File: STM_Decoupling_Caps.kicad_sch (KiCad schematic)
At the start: 11 parts

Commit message: Layout draft complete
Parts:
- added C78: 100 nF, Capacitor_SMD:C_0603_1608Metric, symbol Device:C
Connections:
- net GND: now also C78.1
- new net STM_NRST: C78.2
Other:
- note added: "NRST"
- note added: "VDDA-14"
- note added: "VREF-13"
- title: (none) -> Jakka1
- moved on the sheet: C5, C61, C62, C63, C64, C65, C66, C67, C68, C69, C70

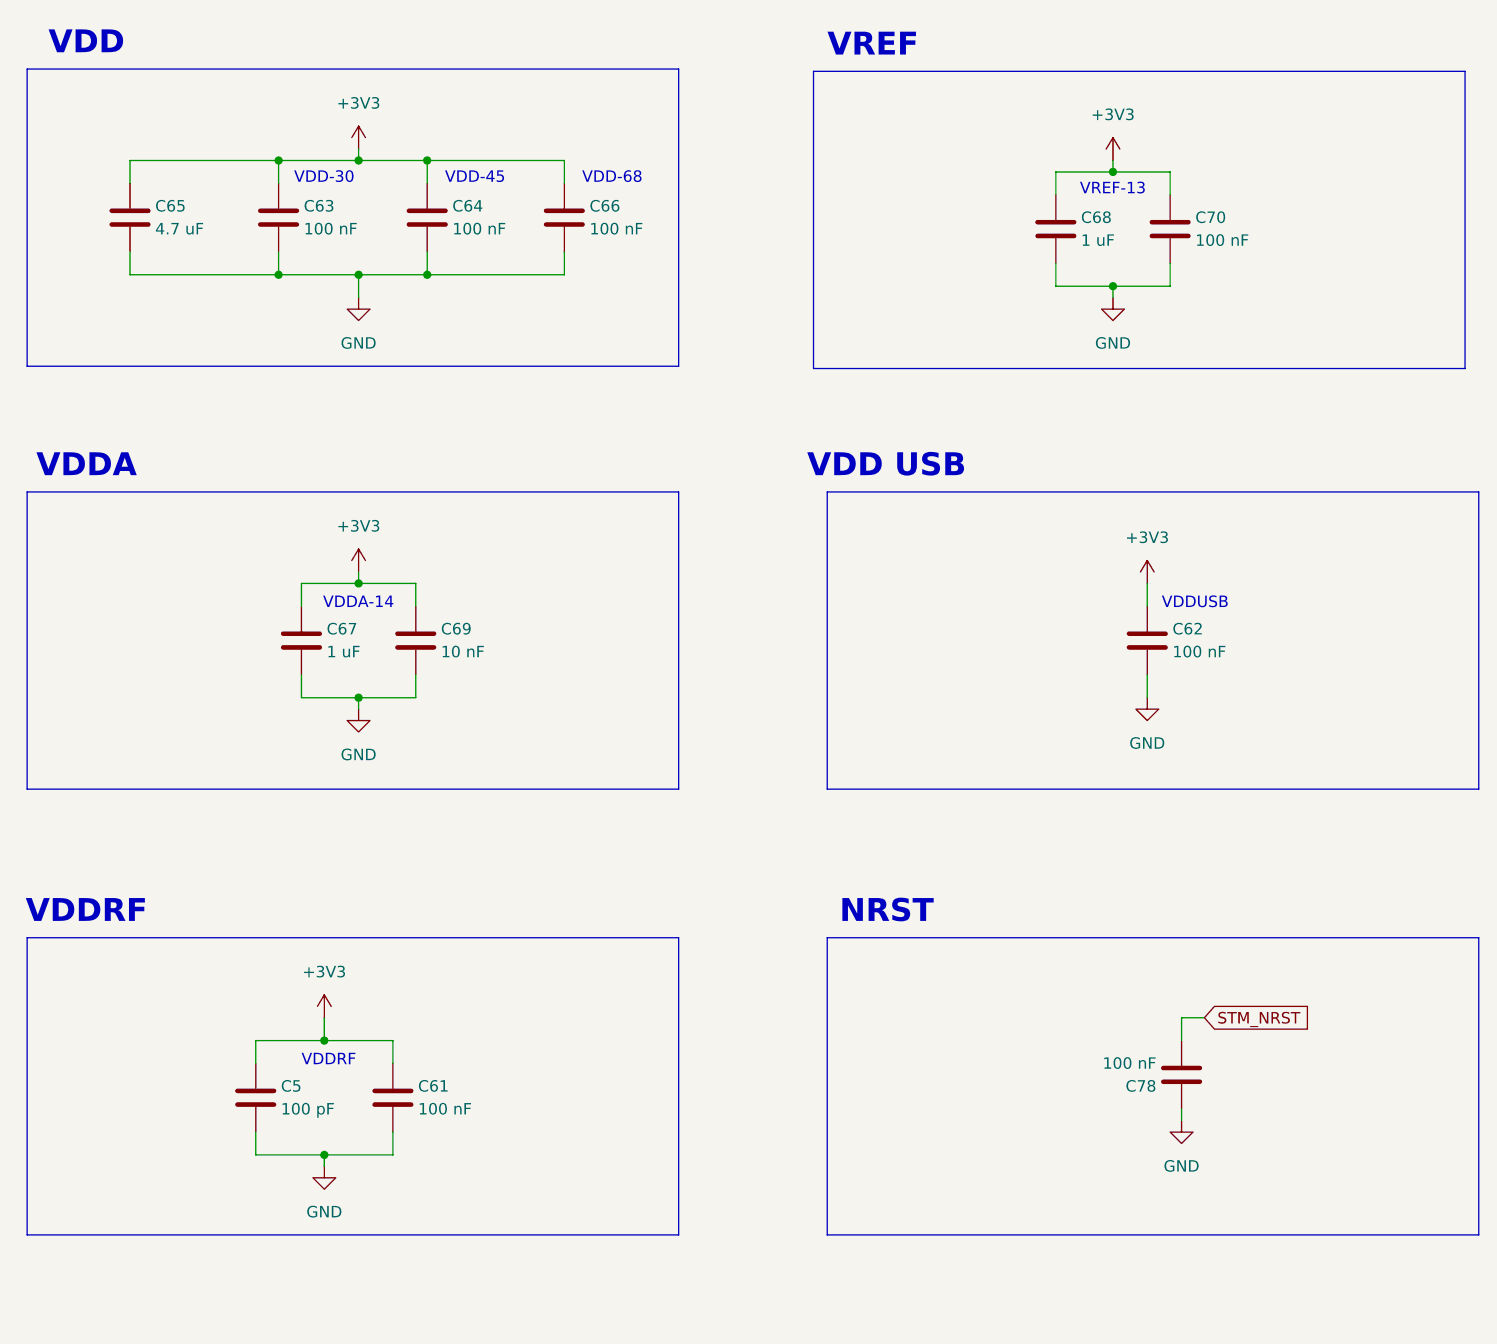
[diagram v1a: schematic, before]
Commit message: First draft of design output, schematic, and layout complete
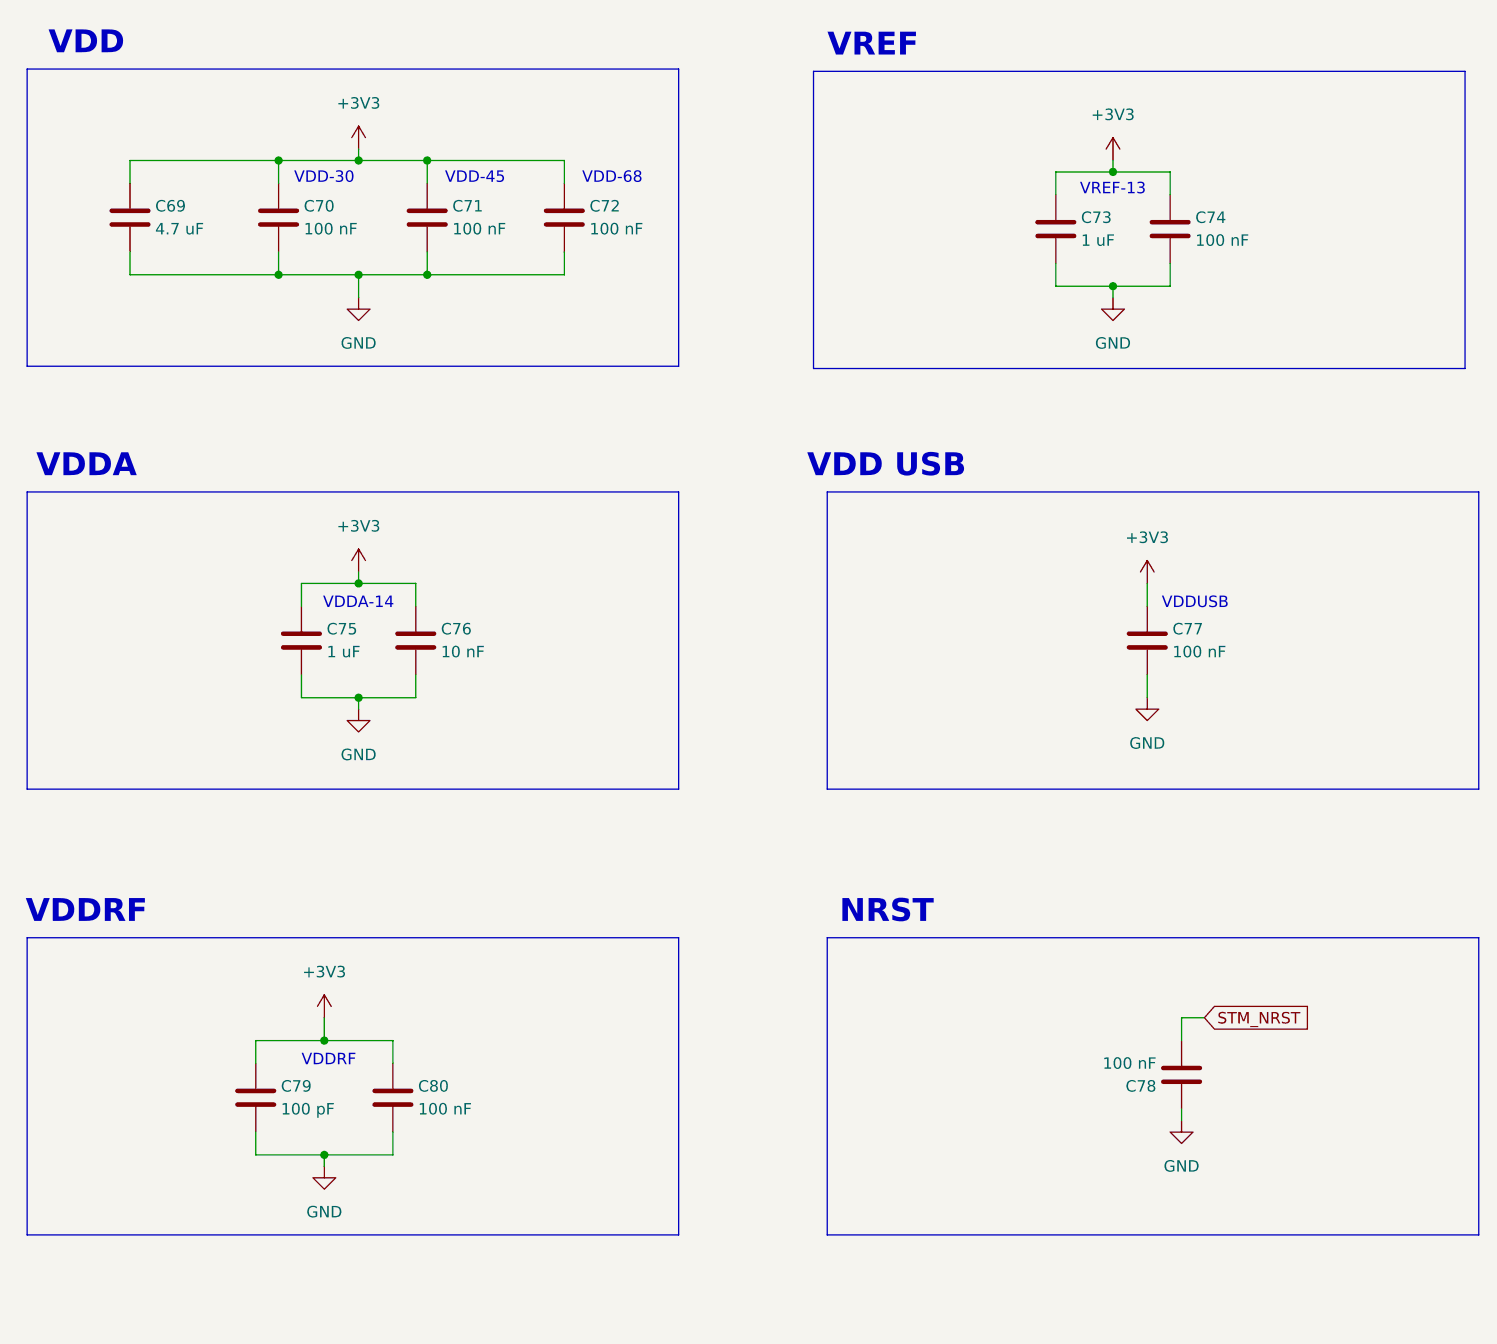
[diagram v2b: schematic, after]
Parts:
- renumbered C65 to C69, C63 to C70, C64 to C71, C66 to C72, C68 to C73, C70 to C74, C67 to C75, C69 to C76, C62 to C77, C5 to C79, C61 to C80
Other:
- company: (none) -> Jacob Kapala
